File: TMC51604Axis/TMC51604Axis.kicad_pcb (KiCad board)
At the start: 2 copper layers, 63 parts, among them Q1 LTC4359IMS8_PBF, Q2 DMHT6016LFJ, Q3 DMHT6016LFJ, Q4 BSS138, U1 TMC5160-TA

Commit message: sync
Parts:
- removed D1, D11, D12, D2, D5, D6, D7, D8: BAT54, digikey-footprints:SOT-23-3
- C10, C2: footprint Capacitor_SMD:C_0805_2012Metric_Pad1.15x1.40mm_HandSolder -> Capacitor_SMD:C_0603_1608Metric
- C11, C12, C13, C14, C19, C22, C23, C24, C4, C5, C8, C9: footprint Capacitor_SMD:C_0603_1608Metric_Pad1.05x0.95mm_HandSolder -> Capacitor_SMD:C_0603_1608Metric
- C15, C16, C17, C18, C20, C6: footprint Capacitor_SMD:C_1206_3216Metric_Pad1.42x1.75mm_HandSolder -> Capacitor_SMD:C_1206_3216Metric
- D10, D3, D4, D9: footprint Package_TO_SOT_SMD:SOT-23_Handsoldering -> Package_TO_SOT_SMD:SOT-23
- R1: footprint Resistor_SMD:R_1210_3225Metric_Pad1.42x2.65mm_HandSolder -> Resistor_SMD:R_1210_3225Metric
- R10, R19: footprint Resistor_SMD:R_2512_6332Metric_Pad1.52x3.35mm_HandSolder -> Resistor_SMD:R_2512_6332Metric
- R11, R12, R13, R14, R15, R16, R17, R18, R2, R20, R21, R22, R3, R4, R5, R6, R7, R8, R9: footprint Resistor_SMD:R_0805_2012Metric_Pad1.15x1.40mm_HandSolder -> Resistor_SMD:R_0603_1608Metric_Pad1.05x0.95mm_HandSolder
- moved R5 95.4 mm to (182.8, 68.5), turned to 270 degrees
- moved R15 93.5 mm to (179.8, 85.6), turned to 180 degrees
- moved R17 90.7 mm to (176.0, 86.9)
- moved C22 83.9 mm to (179.8, 81.3), turned to 180 degrees
- moved R16 83.6 mm to (179.8, 83.6)
- moved C7 81.0 mm to (55.4, 53.0)
- moved R12 79.6 mm to (176.0, 82.8)
- moved R14 76.5 mm to (176.0, 84.8)
- moved R3 74.8 mm to (176.8, 65.5), turned to 180 degrees
- moved C19 74.5 mm to (162.6, 88.5), turned to 90 degrees
- moved R8 73.5 mm to (180.6, 72.6), turned to 180 degrees
- moved R4 73.0 mm to (180.0, 57.5)
- moved C2 67.9 mm to (158.2, 88.8), turned to 90 degrees
- moved R13 66.8 mm to (164.5, 88.5), turned to 90 degrees
- moved R7 63.5 mm to (171.3, 66.3), turned to 0 degrees
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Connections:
- U1 pad 49: GND -> (no net)
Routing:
- net GND: track 20.2 -> 0.00 mm
- net /MotorDrv1/HB1: track 6.21 -> 0.00 mm
- net Net-(Q2-Pad1): track 7.54 -> 1.98 mm
- net Net-(C3-Pad2): track 0.00 -> 4.90 mm
- net Net-(Q2-Pad4): track 0.00 -> 4.78 mm
- net Net-(C2-Pad1): track 0.00 -> 4.62 mm
- net /MotorDrv1/HA2: track 0.00 -> 4.36 mm
- net +VMotor: track 0.00 -> 4.17 mm
- net Net-(C9-Pad2): track 3.75 -> 0.00 mm
- net Net-(C3-Pad1): track 0.00 -> 3.71 mm
- net Net-(Q3-Pad12): track 0.00 -> 3.50 mm
- net Net-(C2-Pad2): track 0.00 -> 3.05 mm
- net Net-(C19-Pad2): track 0.00 -> 3.04 mm
- net /MotorDrv1/StepperA: track 2.51 -> 0.00 mm
- net Net-(Q2-Pad9): track 0.00 -> 2.33 mm
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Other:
- net class Default: trace_width 0.25 -> 0.28

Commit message: sync
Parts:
- moved R13 22.9 mm to (183.8, 76.1), turned to 180 degrees
- moved Q3 19.1 mm to (184.0, 80.4)
- moved C19 18.7 mm to (151.8, 73.2)
- moved C2 18.7 mm to (147.4, 73.6)
- moved C3 18.7 mm to (149.7, 73.4)
- moved R17 13.0 mm to (186.9, 94.0)
- moved C22 13.0 mm to (190.8, 88.4)
- moved R16 13.0 mm to (190.8, 90.7)
- moved R4 6.65 mm to (183.1, 63.4)
- moved R8 6.52 mm to (175.1, 69.1), turned to 0 degrees
- moved R14 6.04 mm to (178.3, 79.2)
- moved R3 5.01 mm to (179.3, 69.8)
- moved Q2 4.95 mm to (184.1, 67.8)
- moved R2 4.95 mm to (179.2, 65.8)
- moved R5 4.10 mm to (183.3, 72.5), turned to 180 degrees
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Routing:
- net /MotorDrv1/LB1: track 0.00 -> 18.5 mm, vias 0 -> 2
- net /MotorDrv1/LB2: track 0.00 -> 16.9 mm, vias 0 -> 2
- net /MotorDrv1/StepperA: track 0.00 -> 11.3 mm
- net /MotorDrv1/HB2: track 0.00 -> 10.9 mm, vias 0 -> 2
- net /MotorDrv1/StepperB: track 0.00 -> 10.9 mm
- net /MotorDrv1/HB1: track 0.00 -> 10.7 mm, vias 0 -> 2
- net Net-(C9-Pad2): track 0.00 -> 8.27 mm
- net Net-(R8-Pad1): track 0.00 -> 6.60 mm
- net Net-(R7-Pad1): track 0.00 -> 6.23 mm
- net Net-(C5-Pad2): track 0.00 -> 4.94 mm
- net Net-(Q2-Pad4): track 4.78 -> 2.57 mm

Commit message: Layout done! Still untested
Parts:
- removed C8: 10uF, Capacitor_SMD:C_0603_1608Metric
- added C25: 2.2u, Capacitor_SMD:C_0603_1608Metric, F.Cu at (104.4, 92.5)
- added C26: 470n, Capacitor_SMD:C_0603_1608Metric, F.Cu at (102.5, 109.0)
- added C27: 100n, Capacitor_SMD:C_0603_1608Metric, F.Cu at (96.5, 101.5)
- added C28: 1n/100V, Capacitor_SMD:C_0603_1608Metric, B.Cu at (136.4, 94.9)
- added C29: 1n/100V, Capacitor_SMD:C_0603_1608Metric, B.Cu at (136.7, 98.9)
- added C30: 1n/100V, Capacitor_SMD:C_0603_1608Metric, B.Cu at (136.7, 103.3)
- added C31: 1n/100V, Capacitor_SMD:C_0603_1608Metric, B.Cu at (136.3, 107.4)
- added C32: 2n2, Capacitor_SMD:C_0603_1608Metric, F.Cu at (116.5, 88.5)
- added C33: 100n, Capacitor_SMD:C_0603_1608Metric, F.Cu at (129.4, 89.2)
- added C34: 100n, Capacitor_SMD:C_0603_1608Metric, F.Cu at (94.4, 92.6)
- added C35: 470n, Capacitor_SMD:C_0603_1608Metric, F.Cu at (113.5, 109.6)
- added C36: 470n, Capacitor_SMD:C_0603_1608Metric, F.Cu at (113.5, 102.9)
- added C37: 15pF, peters:D_0805_peter, F.Cu at (98.2, 90.9)
- added C38: 470n/100V, Capacitor_SMD:C_1206_3216Metric, F.Cu at (118.5, 106.2)
- added C39: 220uF/100V, Capacitor_SMD:CP_Elec_10x14.3, F.Cu at (122.4, 121.7)
- added C40: 2n2, Capacitor_SMD:C_0603_1608Metric, F.Cu at (116.3, 113.5)
- added C41: 100n, Capacitor_SMD:C_0603_1608Metric, F.Cu at (130.0, 112.6)
- added C42: 10u, peters:C_0805_peter, B.Cu at (85.6, 125.7)
- added C43: 100n, peters:C_0805_peter, B.Cu at (109.1, 114.4)
- added C44: 100n, peters:C_0805_peter, B.Cu at (91.8, 103.6)
- added C45: 100n, peters:C_0805_peter, B.Cu at (95.2, 114.6)
- added D1: 1N4148W, Diode_SMD:D_SOD-123, B.Cu at (101.1, 76.2)
- added D11: LED, peters:D_0805__HandSolder_peter, F.Cu at (80.8, 97.9)
- added D12: LED, peters:D_0805__HandSolder_peter, F.Cu at (85.7, 97.9)
- added D13: LED, peters:D_0805__HandSolder_peter, F.Cu at (88.1, 97.9)
- added D14: LED, peters:D_0805__HandSolder_peter, F.Cu at (83.2, 97.9)
- added D15: LED, peters:D_0805__HandSolder_peter, F.Cu at (90.0, 118.5)
- added D16: LED, peters:D_0805__HandSolder_peter, F.Cu at (82.8, 118.5)
- added D17: LED, peters:D_0805__HandSolder_peter, F.Cu at (80.4, 118.5)
- added D18: LED, peters:D_0805__HandSolder_peter, F.Cu at (85.2, 118.5)
- added D19: LED, peters:D_0805__HandSolder_peter, F.Cu at (87.6, 118.5)
- added D2: 7V, Diode_SMD:D_1206_3216Metric, B.Cu at (106.6, 76.2)
- added D20: BAT54S, Package_TO_SOT_SMD:SOT-23, B.Cu at (78.0, 110.4)
- added D21: BAT54S, Package_TO_SOT_SMD:SOT-23, B.Cu at (81.4, 101.7)
- added D22: BAT54S, Package_TO_SOT_SMD:SOT-23, B.Cu at (77.6, 90.0)
- added D23: BAT54S, Package_TO_SOT_SMD:SOT-23, B.Cu at (81.4, 90.0)
- added D24: BAT54S, Package_TO_SOT_SMD:SOT-23, B.Cu at (77.3, 101.7)
- added D25: BAT54S, Package_TO_SOT_SMD:SOT-23, B.Cu at (86.5, 121.8)
- added D26: BAT54S, Package_TO_SOT_SMD:SOT-23, B.Cu at (77.5, 122.4)
- added D27: BAT54S, Package_TO_SOT_SMD:SOT-23, B.Cu at (91.1, 121.8)
- added D28: BAT54S, Package_TO_SOT_SMD:SOT-23, B.Cu at (95.6, 121.8)
- added D29: BAT54S, Package_TO_SOT_SMD:SOT-23, B.Cu at (81.5, 122.4)
- added D5: LT1766, Package_SO:TSSOP-16-1EP_4.4x5mm_P0.65mm, B.Cu at (92.5, 71.5)
- added D6: D_Schottky, Diode_SMD:D_SOD-123F, B.Cu at (92.6, 66.5)
- added D7: ZHCS1006TA, Package_TO_SOT_SMD:SOT-23, F.Cu at (107.7, 88.3)
- added D8: ZHCS1006TA, Package_TO_SOT_SMD:SOT-23, F.Cu at (111.5, 88.3)
- added F1: Fuse, Fuse:Fuse_2512_6332Metric, F.Cu at (80.6, 76.2)
- added FB2: MPZ2012S601A, Resistor_SMD:R_0805_2012Metric_Pad1.15x1.40mm_HandSolder, B.Cu at (91.7, 76.8)
- added H1: MountingHole, MountingHole:MountingHole_3.2mm_M3, F.Cu at (81.7, 66.9)
- added H2: MountingHole, MountingHole:MountingHole_3.2mm_M3, F.Cu at (134.4, 130.6)
- added H3: MountingHole, MountingHole:MountingHole_3.2mm_M3, F.Cu at (134.4, 66.9)
- added H4: MountingHole, MountingHole:MountingHole_3.2mm_M3, F.Cu at (64.4, 130.6)
- added J1: +48Vin, Connector_Phoenix_MSTB:PhoenixContact_MSTB_2,5_2-GF_1x02_P5.00mm_Horizontal_ThreadedFlange_MountHole, F.Cu at (71.1, 70.9)
- added J2: Stepper_conn, TerminalBlock_Phoenix:TerminalBlock_Phoenix_PT-1,5-4-3.5-H_1x04_P3.50mm_Horizontal, F.Cu at (133.9, 95.9)
- added J3: RJ45_Shielded, peters:360s-1812-11001(RJ45), F.Cu at (69.3, 115.6)
- added J4: EncCon1, TerminalBlock_Phoenix:TerminalBlock_Phoenix_PT-1,5-3-3.5-H_1x03_P3.50mm_Horizontal, F.Cu at (92.2, 130.2)
- added J5: RJ45_Shielded, peters:360s-1812-11001(RJ45), F.Cu at (69.3, 95.4)
- added J6: EncCon2, TerminalBlock_Phoenix:TerminalBlock_Phoenix_PT-1,5-3-3.5-H_1x03_P3.50mm_Horizontal, F.Cu at (103.9, 130.2)
- added JP1: SPI_MODE, Jumper:SolderJumper-3_P2.0mm_Open_TrianglePad1.0x1.5mm, F.Cu at (123.1, 129.9)
- added JP2: SD_MODE, Jumper:SolderJumper-3_P2.0mm_Open_TrianglePad1.0x1.5mm, F.Cu at (111.4, 129.8)
- added JP3: Encoder_Voltage_Sel, Jumper:SolderJumper-3_P2.0mm_Open_TrianglePad1.0x1.5mm, F.Cu at (75.8, 129.9)
- added L1: 33uH, Inductor_SMD:L_7.3x7.3_H3.5, B.Cu at (105.0, 70.1)
- added R23: 12R, Resistor_SMD:R_0603_1608Metric, F.Cu at (119.5, 108.3)
- added R24: 12R, Resistor_SMD:R_0603_1608Metric, F.Cu at (119.5, 101.9)
- added R25: 12R, Resistor_SMD:R_0603_1608Metric, F.Cu at (119.5, 110.6)
- added R26: 47R, Resistor_SMD:R_0603_1608Metric, F.Cu at (119.5, 112.5)
- added R27: 0R1, Resistor_SMD:R_1206_3216Metric, F.Cu at (126.9, 112.8)
- added R28: 47R, Resistor_SMD:R_0603_1608Metric, F.Cu at (119.5, 114.6)
- added R29: 100K, Resistor_SMD:R_0603_1608Metric, F.Cu at (99.2, 110.6)
- added R30: 100K, Resistor_SMD:R_0603_1608Metric, F.Cu at (96.0, 113.2)
- added R31: 2k2, peters:R_0805_peter, F.Cu at (80.8, 102.9)
- added R32: 2k2, peters:R_0805_peter, F.Cu at (85.7, 102.9)
- added R33: 100R, peters:R_0805_peter, B.Cu at (73.2, 113.3)
- added R34: 100R, peters:R_0805_peter, B.Cu at (73.4, 97.3)
- added R35: 100R, peters:R_0805_peter, B.Cu at (73.4, 92.8)
- added R36: 100R, peters:R_0805_peter, B.Cu at (73.4, 95.1)
- added R37: 100R, peters:R_0805_peter, B.Cu at (73.4, 99.6)
- added R38: 100R, peters:R_0805_peter, B.Cu at (88.8, 125.7)
- added R39: 100R, peters:R_0805_peter, B.Cu at (72.9, 119.9)
- added R40: 100R, peters:R_0805_peter, B.Cu at (92.3, 125.7)
- added R41: 2k2, peters:R_0805_peter, F.Cu at (88.1, 102.9)
- added R42: 2k2, peters:R_0805_peter, F.Cu at (83.3, 102.9)
- added R43: 2k2, peters:R_0805_peter, F.Cu at (90.0, 122.7)
- added R44: 2k2, peters:R_0805_peter, F.Cu at (82.7, 122.7)
- added R45: 2k2, peters:R_0805_peter, F.Cu at (80.4, 122.7)
- added R46: 2k2, peters:R_0805_peter, F.Cu at (85.2, 122.7)
- added R47: 2k2, peters:R_0805_peter, F.Cu at (87.6, 122.7)
- added R48: 100R, peters:R_0805_peter, B.Cu at (97.2, 125.6)
- added R49: 100R, peters:R_0805_peter, B.Cu at (72.9, 117.6)
- added TP1: TestPoint, TestPoint:TestPoint_Pad_1.5x1.5mm, F.Cu at (86.7, 70.9)
- added TP2: TestPoint, TestPoint:TestPoint_Pad_1.5x1.5mm, F.Cu at (92.8, 70.9)
- added TP3: spare, TestPoint:TestPoint_THTPad_1.0x1.0mm_Drill0.5mm, F.Cu at (100.5, 123.2)
- added TP4: TestPoint, TestPoint:TestPoint_Pad_1.5x1.5mm, F.Cu at (108.3, 82.8)
- added TP5: TestPoint, TestPoint:TestPoint_Pad_1.5x1.5mm, F.Cu at (101.2, 82.8)
- added TP6: TestPoint, TestPoint:TestPoint_Pad_1.5x1.5mm, F.Cu at (104.5, 82.8)
- added TP7: TestPoint, TestPoint:TestPoint_Pad_1.5x1.5mm, F.Cu at (112.3, 82.7)
- added U2: LM2937, Package_TO_SOT_SMD:SOT-223-3_TabPin2, B.Cu at (82.8, 81.8)
- added U3: TMC5160A-TA, peters:LQFP-48-1EP_7x7mm_P0.5mm_EP3.6x3.6mm_peter, F.Cu at (104.3, 100.7)
- added U4: ASDMB-12.0MHz, Oscillator:Oscillator_SMD_Abracon_ASDMB-4Pin_2.5x2.0mm, F.Cu at (98.3, 93.9)
- added U5: 74LVC125, Package_SO:SO-14_5.3x10.2mm_P1.27mm, B.Cu at (102.6, 111.8)
- added U6: 74LVC125, Package_SO:SO-14_5.3x10.2mm_P1.27mm, B.Cu at (88.9, 96.8)
- added U7: 74LVC125, Package_SO:SO-14_5.3x10.2mm_P1.27mm, B.Cu at (88.9, 111.6)
- C1: value 4,7uF -> 330n; footprint Capacitor_SMD:C_1210_3225Metric_Pad1.42x2.65mm_HandSolder -> peters:C_0805_peter; moved to B.Cu
- C10: value 2.2u -> 10u; moved to B.Cu
- C11: value 470n -> 1uF; footprint Capacitor_SMD:C_0603_1608Metric -> peters:C_0805_peter; moved to B.Cu
- C12: value 100n -> 100p; footprint Capacitor_SMD:C_0603_1608Metric -> peters:C_0805_peter; moved to B.Cu
- C13: value 2n2 -> 220p; footprint Capacitor_SMD:C_0603_1608Metric -> peters:C_0805_peter; moved to B.Cu
- C14: value 100n -> 22nF; footprint Capacitor_SMD:C_0603_1608Metric -> peters:C_0805_peter; moved to B.Cu
- C15: value 1n/100V -> 100n/100v; footprint Capacitor_SMD:C_1206_3216Metric -> Capacitor_SMD:C_1210_3225Metric_Pad1.42x2.65mm_HandSolder
- C16: value 1n/100V -> 4,7uF/100v; footprint Capacitor_SMD:C_1206_3216Metric -> Capacitor_SMD:C_1210_3225Metric_Pad1.42x2.65mm_HandSolder
- C17: value 1n/100V -> 22n/100v; footprint Capacitor_SMD:C_1206_3216Metric -> Capacitor_SMD:C_0603_1608Metric
- C18: value 1n/100V -> 100n/100V; footprint Capacitor_SMD:C_1206_3216Metric -> peters:C_0805_peter
- C19: value 470n -> 220n/100v
- C2: value 22n/100v -> 10p; footprint Capacitor_SMD:C_0603_1608Metric -> peters:C_0805_peter
- C21: footprint Capacitor_THT:C_Radial_D16.0mm_H25.0mm_P7.50mm -> Capacitor_SMD:CP_Elec_10x14.3
- C23: value 2n2 -> 2.2uF
- C24: value 100n -> 470n
- C3: value 100n/100V -> 10uF/100v; footprint Capacitor_SMD:C_0805_2012Metric_Pad1.15x1.40mm_HandSolder -> Capacitor_SMD:CP_Elec_8x6.2
- C4: value 220n -> 22uF/100v; footprint Capacitor_SMD:C_0603_1608Metric -> Capacitor_SMD:CP_Elec_8x6.2
- C5: value 470n -> 47nF; footprint Capacitor_SMD:C_0603_1608Metric -> peters:C_0805_peter
- C6: value 470n/100V -> 2.2uF; footprint Capacitor_SMD:C_1206_3216Metric -> peters:C_0805_peter; moved to B.Cu
- C7: value 220uF/100V -> 47u/25V; footprint Capacitor_THT:C_Radial_D16.0mm_H25.0mm_P7.50mm -> Capacitor_THT:CP_Radial_D10.0mm_P5.00mm
- C9: value 470n -> 100n; moved to B.Cu
- D3: value ZHCS1006TA -> 10V; footprint Package_TO_SOT_SMD:SOT-23 -> Diode_SMD:D_1206_3216Metric
- D4: value ZHCS1006TA -> LED; footprint Package_TO_SOT_SMD:SOT-23 -> Diode_SMD:D_0805_2012Metric
- Q1: value LTC4359IMS8_PBF -> SUD08P06-155L; footprint digikey-footprints:TSSOP-8_W3mm -> Package_TO_SOT_SMD:TO-252-2
- R1: value 1R -> 0R01; footprint Resistor_SMD:R_1210_3225Metric -> Resistor_SMD:R_2512_6332Metric
- R10: value 0R1 -> 12R; footprint Resistor_SMD:R_2512_6332Metric -> Resistor_SMD:R_0603_1608Metric
- R11: value 47R -> 12R; footprint Resistor_SMD:R_0603_1608Metric_Pad1.05x0.95mm_HandSolder -> Resistor_SMD:R_0603_1608Metric
- R12: value 12R -> 0R; footprint Resistor_SMD:R_0603_1608Metric_Pad1.05x0.95mm_HandSolder -> Resistor_SMD:R_0603_1608Metric
- R13, R14: footprint Resistor_SMD:R_0603_1608Metric_Pad1.05x0.95mm_HandSolder -> Resistor_SMD:R_0603_1608Metric
- R15: value 12R -> 47R; footprint Resistor_SMD:R_0603_1608Metric_Pad1.05x0.95mm_HandSolder -> Resistor_SMD:R_0603_1608Metric
- R16: value 0R -> 0R1; footprint Resistor_SMD:R_0603_1608Metric_Pad1.05x0.95mm_HandSolder -> Resistor_SMD:R_1206_3216Metric
- R17: value 0R -> 47R; footprint Resistor_SMD:R_0603_1608Metric_Pad1.05x0.95mm_HandSolder -> Resistor_SMD:R_0603_1608Metric
- R18: value 47R -> 100k; footprint Resistor_SMD:R_0603_1608Metric_Pad1.05x0.95mm_HandSolder -> peters:R_0805_peter
- R19: value 0R1 -> NC; footprint Resistor_SMD:R_2512_6332Metric -> peters:R_0805_peter
- R2: value 12R -> 36K5; footprint Resistor_SMD:R_0603_1608Metric_Pad1.05x0.95mm_HandSolder -> peters:R_0805_peter; moved to B.Cu
- R20, R9: value 47R -> 0R; footprint Resistor_SMD:R_0603_1608Metric_Pad1.05x0.95mm_HandSolder -> Resistor_SMD:R_0603_1608Metric
- R21: value 100K -> 0R; footprint Resistor_SMD:R_0603_1608Metric_Pad1.05x0.95mm_HandSolder -> Resistor_SMD:R_0603_1608Metric
- R22: value 100K -> 12R; footprint Resistor_SMD:R_0603_1608Metric_Pad1.05x0.95mm_HandSolder -> Resistor_SMD:R_0603_1608Metric
- R3: value 12R -> 100k; footprint Resistor_SMD:R_0603_1608Metric_Pad1.05x0.95mm_HandSolder -> peters:R_0805_peter
- R4: value 12R -> 10K; footprint Resistor_SMD:R_0603_1608Metric_Pad1.05x0.95mm_HandSolder -> peters:R_0805_peter
- R5: value 12R -> 4K12; footprint Resistor_SMD:R_0603_1608Metric_Pad1.05x0.95mm_HandSolder -> peters:R_0805_peter; moved to B.Cu
- R6: value 2R2 -> 2k2; footprint Resistor_SMD:R_0603_1608Metric_Pad1.05x0.95mm_HandSolder -> peters:R_0805_peter; moved to B.Cu
- R7: value 0R -> 1R; footprint Resistor_SMD:R_0603_1608Metric_Pad1.05x0.95mm_HandSolder -> peters:R_0805_peter
- R8: value 0R -> 2R2; footprint Resistor_SMD:R_0603_1608Metric_Pad1.05x0.95mm_HandSolder -> Resistor_SMD:R_0603_1608Metric
- U1: value TMC5160-TA -> AP2210-3.3V; footprint Package_QFP:TQFP-48-1EP_7x7mm_P0.5mm_EP5x5mm_ThermalVias -> Package_TO_SOT_SMD:SOT-23-5_HandSoldering; moved to B.Cu
- moved R5 98.9 mm to (84.3, 72.5), turned to 270 degrees
- moved R4 93.0 mm to (90.2, 65.4)
- moved R2 92.8 mm to (86.6, 72.5), turned to 90 degrees
- moved C9 90.0 mm to (85.6, 76.5)
- moved R3 89.7 mm to (91.7, 89.0), turned to 0 degrees
- moved R7 85.9 mm to (102.6, 113.3), turned to 270 degrees
- moved C5 84.2 mm to (92.1, 83.4)
- moved C22 77.9 mm to (113.7, 99.3)
- moved R8 76.1 mm to (102.7, 92.6), turned to 90 degrees
- moved Q4 75.4 mm to (98.9, 113.3)
- moved C15 75.4 mm to (105.2, 118.4), turned to 270 degrees
- moved U1 74.5 mm to (91.6, 81.2), turned to 0 degrees
- moved R17 67.7 mm to (119.5, 87.6), turned to 180 degrees
- moved C21 67.7 mm to (122.4, 80.6)
- moved R13 66.0 mm to (119.5, 91.3), turned to 0 degrees
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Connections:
- C1 pad 1: +VMotor -> Net-(C1-Pad1)
- C1 pad 2: GND -> Net-(C1-Pad2)
- C10 pad 1: Net-(C10-Pad1) -> +5V
- C11 pad 1: Net-(C11-Pad1) -> +5V
- C12 pad 1: GND -> Net-(C12-Pad1)
- C12 pad 2: +3V3 -> GND
- C13 pad 2: Net-(C13-Pad2) -> GND
- C14 pad 1: GND -> Net-(C14-Pad1)
- C14 pad 2: Net-(C14-Pad2) -> GND
- C15 pad 1: /MotorDrv1/StepperA -> +48V
- C16 pad 1: /MotorDrv1/StepperB -> +48V
- C17 pad 1: /MotorDrv1/StepperC -> Net-(C17-Pad1)
- C17 pad 2: GND -> Net-(C17-Pad2)
- C18 pad 1: /MotorDrv1/StepperD -> Net-(C18-Pad1)
- C18 pad 2: GND -> Net-(C18-Pad2)
- C19 pad 1: /MotorDrv1/StepperD -> Net-(C18-Pad1)
- C19 pad 2: Net-(C19-Pad2) -> GND
- C2 pad 1: Net-(C2-Pad1) -> +48V
- C20 pad 1: +VMotor -> +48V
- C21 pad 1: +VMotor -> +48V
- C22 pad 1: /MotorDrv1/StepperC -> /MotorDrv1/StepperB
- C23 pad 1: Net-(C23-Pad1) -> +12V
- C23 pad 2: Net-(C23-Pad2) -> GND
- C24 pad 1: GND -> /MotorDrv1/StepperA
- C3 pad 1: Net-(C3-Pad1) -> +48V
- C3 pad 2: Net-(C3-Pad2) -> GND
- C4 pad 1: Net-(C3-Pad1) -> +48V
- C5 pad 1: /MotorDrv1/StepperB -> Net-(C2-Pad2)
- C5 pad 2: Net-(C5-Pad2) -> GND
- C6 pad 1: +VMotor -> +3V3
- C7 pad 1: +VMotor -> +12V
- C9 pad 1: /MotorDrv1/StepperA -> Net-(C9-Pad1)
- C9 pad 2: Net-(C9-Pad2) -> GND
- D3 pad 1: /MotorDrv1/StepperB -> Net-(C2-Pad2)
- D3 pad 2: (no net) -> Net-(D3-Pad2)
- D4 pad 1: /MotorDrv1/StepperA -> Net-(D4-Pad1)
- D4 pad 2: (no net) -> +48V
- Q1 pad 1: (no net) -> Net-(D3-Pad2)
- Q1 pad 2: (no net) -> Net-(F1-Pad1)
- Q1 pad 3: (no net) -> Net-(C2-Pad2)
- Q2 pad 11: +VMotor -> +48V
- Q2 pad 13: +VMotor -> +48V
- Q2 pad 2: +VMotor -> +48V
- Q2 pad 5: Net-(C14-Pad2) -> Net-(C33-Pad2)
- Q2 pad 6: Net-(C14-Pad2) -> Net-(C33-Pad2)
- Q2 pad 7: Net-(C14-Pad2) -> Net-(C33-Pad2)
- Q2 pad 8: Net-(C14-Pad2) -> Net-(C33-Pad2)
- Q3 pad 11: +VMotor -> +48V
- Q3 pad 13: +VMotor -> +48V
- Q3 pad 2: +VMotor -> +48V
- Q3 pad 5: Net-(C24-Pad2) -> Net-(C41-Pad2)
- Q3 pad 6: Net-(C24-Pad2) -> Net-(C41-Pad2)
- Q3 pad 7: Net-(C24-Pad2) -> Net-(C41-Pad2)
- Q3 pad 8: Net-(C24-Pad2) -> Net-(C41-Pad2)
- R1 pad 1: +VMotor -> Net-(C2-Pad2)
- R1 pad 2: Net-(C3-Pad1) -> +48V
- R10 pad 1: Net-(C14-Pad2) -> /MotorDrv1/HB1
- R10 pad 2: GND -> Net-(Q2-Pad1)
- R11 pad 1: GND -> Net-(Q2-Pad12)
- R11 pad 2: Net-(C13-Pad1) -> /MotorDrv1/HB2
- R12 pad 1: /MotorDrv1/HA1 -> Net-(R12-Pad1)
- R12 pad 2: Net-(Q3-Pad1) -> /MotorDrv1/StepperB
- R13 pad 1: Net-(Q3-Pad12) -> /MotorDrv1/LB1
- R13 pad 2: /MotorDrv1/HA2 -> Net-(Q2-Pad4)
- R14 pad 1: /MotorDrv1/LA1 -> Net-(Q2-Pad9)
- R14 pad 2: Net-(Q3-Pad4) -> /MotorDrv1/LB2
- R15 pad 1: Net-(Q3-Pad9) -> Net-(C33-Pad2)
- R15 pad 2: /MotorDrv1/LA2 -> Net-(C32-Pad2)
- R16 pad 1: Net-(R16-Pad1) -> Net-(C33-Pad2)
- R16 pad 2: /MotorDrv1/StepperC -> GND
- R17 pad 1: Net-(R17-Pad1) -> GND
- R17 pad 2: /MotorDrv1/StepperD -> Net-(C32-Pad1)
- R18 pad 1: Net-(C24-Pad2) -> +3V3
- R18 pad 2: Net-(C23-Pad2) -> Net-(R18-Pad2)
- R19 pad 1: Net-(C24-Pad2) -> GND
- R19 pad 2: GND -> Net-(C37-Pad1)
- R2 pad 1: /MotorDrv1/HB1 -> +12V
- R2 pad 2: Net-(Q2-Pad1) -> Net-(D5-Pad12)
- R20 pad 1: GND -> Net-(R20-Pad1)
- R20 pad 2: Net-(C23-Pad1) -> /MotorDrv1/StepperC
- R21 pad 1: Net-(Q4-Pad3) -> Net-(R21-Pad1)
- R21 pad 2: +3V3 -> /MotorDrv1/StepperD
- R22 pad 1: GND -> /MotorDrv1/HA1
- R22 pad 2: /MotorDrv1/DRV_ENA -> Net-(Q3-Pad1)
- R3 pad 1: Net-(Q2-Pad12) -> Net-(D3-Pad2)
- R3 pad 2: /MotorDrv1/HB2 -> GND
- R4 pad 1: /MotorDrv1/LB1 -> Net-(D4-Pad1)
- R4 pad 2: Net-(Q2-Pad4) -> GND
- R5 pad 1: Net-(Q2-Pad9) -> Net-(D5-Pad12)
- R5 pad 2: /MotorDrv1/LB2 -> GND
- R6 pad 1: Net-(C10-Pad1) -> Net-(C13-Pad1)
- R6 pad 2: Net-(C11-Pad1) -> Net-(C14-Pad1)
- R7 pad 1: Net-(R7-Pad1) -> Net-(C18-Pad1)
- R7 pad 2: /MotorDrv1/StepperA -> +48V
- R8 pad 1: Net-(R8-Pad1) -> Net-(C25-Pad1)
- R8 pad 2: /MotorDrv1/StepperB -> Net-(C26-Pad1)
- R9 pad 1: Net-(C14-Pad2) -> Net-(R9-Pad1)
- R9 pad 2: Net-(C13-Pad2) -> /MotorDrv1/StepperA
- U1 pad 1: /MotorDrv1/HB1 -> +5V
- U1 pad 2: Net-(C9-Pad2) -> GND
- U1 pad 3: +12V -> +5V
- U1 pad 4: +12V -> Net-(C12-Pad1)
- U1 pad 5: Net-(C10-Pad1) -> +3V3
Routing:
- net GND: track 0.00 -> 292.5 mm, vias 0 -> 125
- net +5V: track 0.00 -> 116.4 mm, vias 0 -> 3
- net +12V: track 0.00 -> 71.1 mm, vias 0 -> 2
- net +48V: track 0.00 -> 62.0 mm, vias 0 -> 58
- net +3V3: track 0.00 -> 56.0 mm, vias 0 -> 21
- net /MotorDrv1/CLK: track 0.00 -> 53.1 mm, vias 0 -> 4
- net /MotorDrv1/StepperC: track 0.00 -> 49.1 mm, vias 0 -> 7
- net Net-(JP1-Pad2): track 0.00 -> 45.9 mm, vias 0 -> 2
- net Net-(C40-Pad1): track 0.00 -> 45.6 mm, vias 0 -> 2
- net /MotorDrv1/REFL_STEP: track 0.00 -> 45.1 mm, vias 0 -> 1
- net /Inputs/DIR_REFR: track 0.00 -> 44.2 mm, vias 0 -> 5
- net Net-(C40-Pad2): track 0.00 -> 42.9 mm, vias 0 -> 2
- net /MotorDrv1/MOSI: track 0.00 -> 42.0 mm, vias 0 -> 1
- net /Inputs/enc_volt: track 0.00 -> 39.3 mm, vias 0 -> 1
- net /MotorDrv1/StepperD: track 0.00 -> 38.0 mm, vias 0 -> 5
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- added copper zone on B.Cu, net +3V3
- added copper zone on In2.Cu, net +3V3
- added copper zone on B.Cu, net +48V
- added copper zone on F.Cu, net +48V
- added copper zone on B.Cu, net /MotorDrv1/StepperA
- added copper zone on B.Cu, net /MotorDrv1/StepperB
- added copper zone on B.Cu, net /MotorDrv1/StepperC
- added copper zone on B.Cu, net /MotorDrv1/StepperD
- added copper zone on B.Cu, net GND
- added copper zone on F.Cu, net GND
- added copper zone on In1.Cu, net GND
- added copper zone on F.Cu, net Net-(C2-Pad2)
- added copper zone on B.Cu, net Net-(C33-Pad2)
- added copper zone on F.Cu, net Net-(C33-Pad2)
- added copper zone on B.Cu, net Net-(C41-Pad2)
- added copper zone on F.Cu, net Net-(C41-Pad2)
- added copper zone on F.Cu, net Net-(F1-Pad1)
- added copper zone on F.Cu, net Net-(F1-Pad2)
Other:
- board outline added: 77.7 x 72.8 mm
- copper layers 2 -> 4
- net class Default: trace_width 0.28 -> 0.25; via_dia 0.8 -> 0.6; via_drill 0.4 -> 0.3
- rule via_min_size: 0.4 -> 0.45
- board text added: "+48VDC IN"
- board text added: "12"
- board text added: "3,3"
- board text added: "3.3"
- board text added: "5"
- board text added: "5.0"
- board text added: "A"
- board text added: "B"
- board text added: "C"
- board text added: "CSN"
- board text added: "D"
- board text added: "DIAG_SWn"
- board text added: "DIAG_SWp"
- board text added: "DIR_REF_R"
- board text added: "ENA"
- board text added: "ENCODER"
- board text added: "ENC_VOLT"
- board text added: "GND"
- board text added: "JLCJLCJLCJLC"
- board text added: "N"
- board text added: "SCK"
- board text added: "SDI"
- board text added: "SDO"
- board text added: "SD_MODE"
- board text added: "SPI"
- board text added: "SPI IN"
- board text added: "SPI_MODE"
- board text added: "STEP/DIR IN"
- board text added: "STEPPER OUT"
- board text added: "STEP_REF_L"
- board text added: "Spare"
- board text added: "VCC"

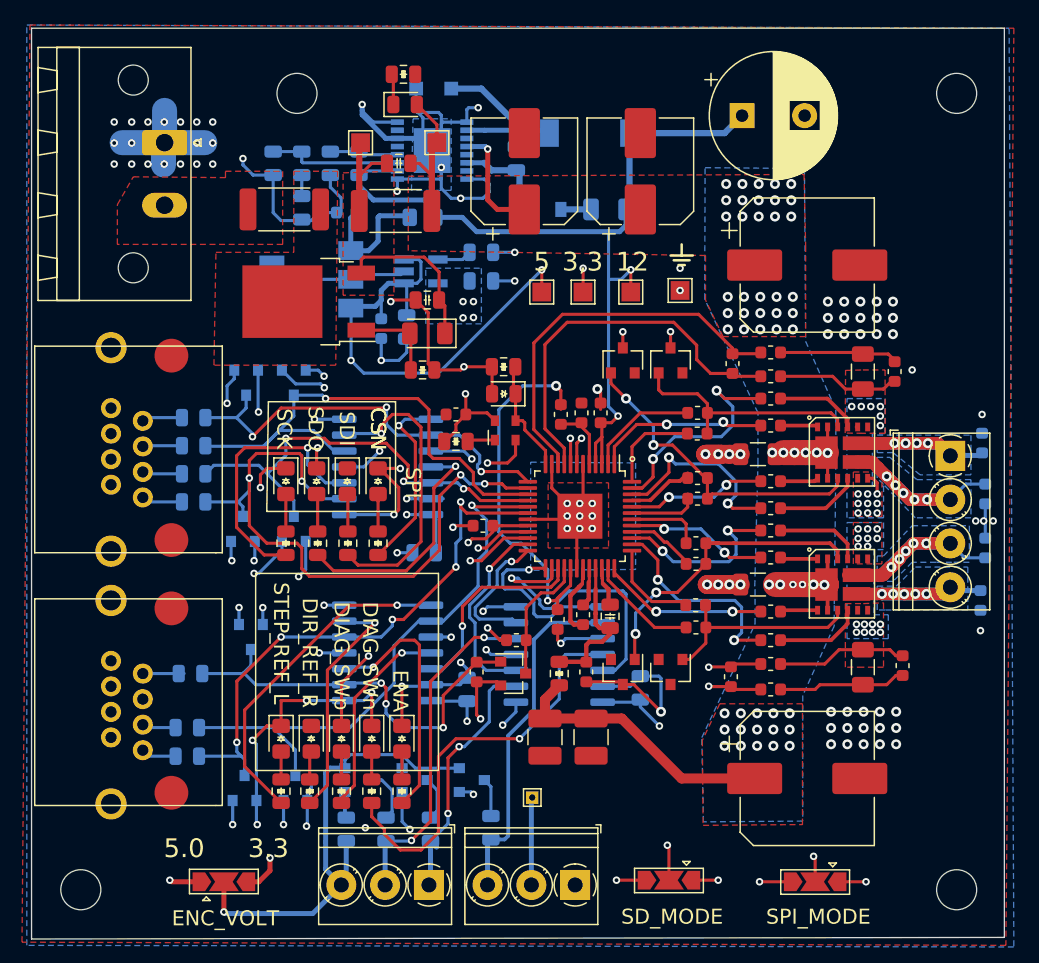
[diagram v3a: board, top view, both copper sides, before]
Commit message: Redone input section
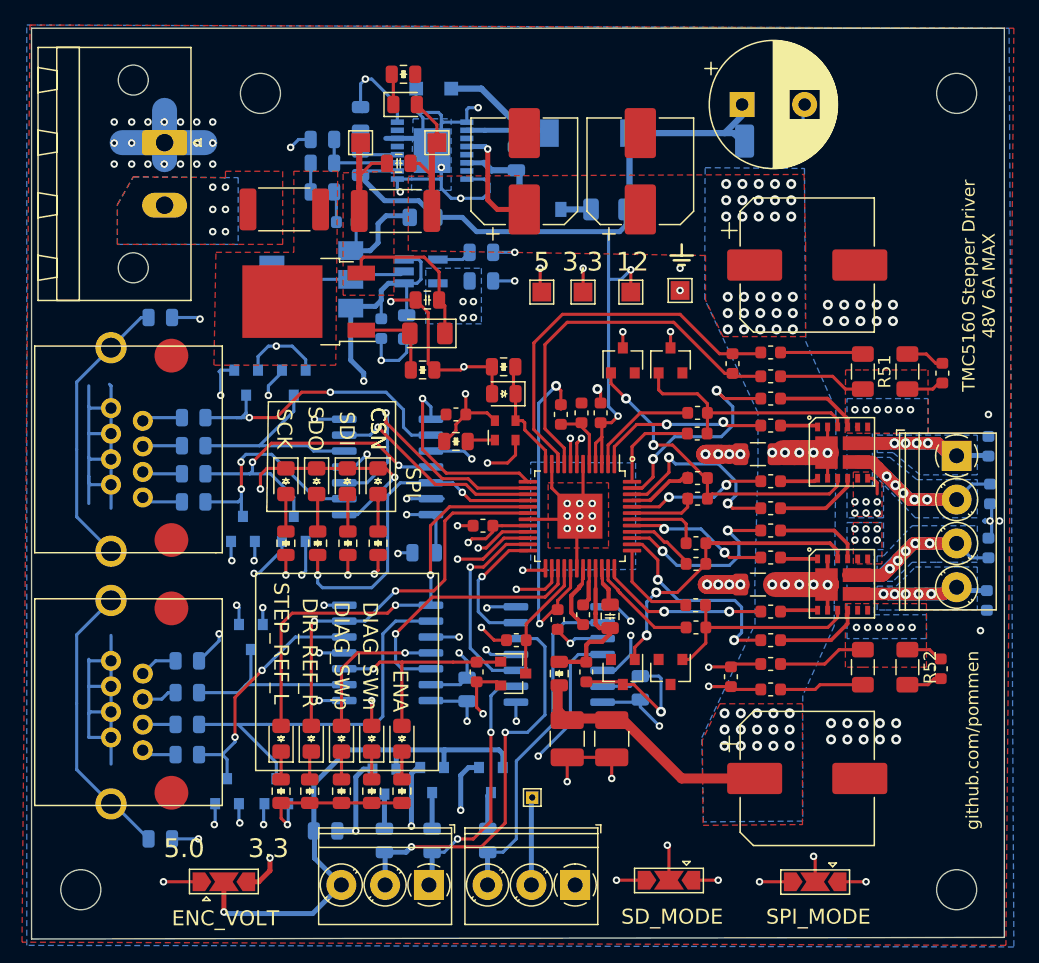
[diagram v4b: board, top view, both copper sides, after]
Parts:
- added C46: 100n, peters:C_0805_peter, B.Cu at (70.7, 126.5)
- added C47: 100n, peters:C_0805_peter, B.Cu at (70.7, 84.8)
- added C8: 47u/25, Capacitor_SMD:C_2010_5025Metric_Pad1.52x2.65mm_HandSolder, B.Cu at (119.8, 70.7)
- added R50: 20R, peters:R_0805_peter, B.Cu at (72.9, 112.3)
- added R51: 0R1, Resistor_SMD:R_1206_3216Metric, F.Cu at (130.4, 89.2)
- added R52: 0R1, Resistor_SMD:R_1206_3216Metric, F.Cu at (130.4, 112.8)
- moved C13 4.37 mm to (83.7, 70.6), turned to 180 degrees
- moved R5 4.30 mm to (86.7, 69.0), turned to 90 degrees
- moved C33 3.81 mm to (133.2, 89.3)
- moved C41 3.06 mm to (133.1, 112.9)
- moved H1 2.92 mm to (78.7, 66.9)
- moved D25 2.16 mm to (88.6, 121.9), turned to 270 degrees
- moved C14 2.08 mm to (83.7, 74.8), turned to 0 degrees
- moved C16 1.78 mm to (103.3, 118.5)
- moved C15 1.66 mm to (106.8, 118.5)
- moved C42 1.66 mm to (83.9, 125.9), turned to 0 degrees
- moved R6 1.65 mm to (83.7, 72.5), turned to 180 degrees
- moved D29 1.55 mm to (80.0, 122.7)
- moved R33 1.55 mm to (72.9, 114.8)
- moved D28 1.52 mm to (97.2, 121.8), turned to 270 degrees
- moved D26 1.42 mm to (76.1, 122.7)
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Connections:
- net /Inputs/DIR_REFR_raw renamed Net-(J3-Pad8)
- net /Inputs/STEP_REFL_raw renamed Net-(J3-Pad6)
- D15 pad 1: GND -> Net-(D15-Pad1)
- D15 pad 2: Net-(D15-Pad2) -> /MotorDrv1/DRV_ENA
- D16 pad 1: GND -> Net-(D16-Pad1)
- D16 pad 2: Net-(D16-Pad2) -> /Inputs/DIR_REFR
- D17 pad 1: GND -> Net-(D17-Pad1)
- D17 pad 2: Net-(D17-Pad2) -> /MotorDrv1/REFL_STEP
- D18 pad 1: GND -> Net-(D18-Pad1)
- D19 pad 1: GND -> Net-(D19-Pad1)
- D20 pad 2: +3V3 -> /Inputs/Signal_VCC
- D20 pad 3: /MotorDrv1/DRV_ENA -> Net-(D20-Pad3)
- D21 pad 2: +3V3 -> /Inputs/Signal_VCC
- D21 pad 3: /MotorDrv1/MISO -> Net-(D21-Pad3)
- D22 pad 2: +3V3 -> /Inputs/Signal_VCC
- D22 pad 3: /Inputs/CSN -> Net-(D22-Pad3)
- D23 pad 2: +3V3 -> /Inputs/Signal_VCC
- D23 pad 3: /MotorDrv1/MOSI -> Net-(D23-Pad3)
- D24 pad 2: +3V3 -> /Inputs/Signal_VCC
- D24 pad 3: /MotorDrv1/CLK -> Net-(D24-Pad3)
- D26 pad 2: +3V3 -> /Inputs/Signal_VCC
- D26 pad 3: /Inputs/DIR_REFR -> Net-(D26-Pad3)
- D29 pad 2: +3V3 -> /Inputs/Signal_VCC
- D29 pad 3: /MotorDrv1/REFL_STEP -> Net-(D29-Pad3)
- J3 pad 2: /Inputs/DRV_ENN_raw -> Net-(J3-Pad2)
- J3 pad 4: (no net) -> Net-(J3-Pad4)
- J3 pad SH: GND -> Net-(C46-Pad1)
- J5 pad SH: GND -> Net-(C47-Pad1)
- R31 pad 1: Net-(R31-Pad1) -> /MotorDrv1/CLK
- R32 pad 1: Net-(R32-Pad1) -> /MotorDrv1/MOSI
- R33 pad 1: /MotorDrv1/DRV_ENA -> Net-(D20-Pad3)
- R33 pad 2: /Inputs/DRV_ENN_raw -> Net-(J3-Pad4)
- R34 pad 1: /MotorDrv1/MISO -> Net-(D21-Pad3)
- R35 pad 1: /Inputs/CSN -> Net-(D22-Pad3)
- R36 pad 1: /MotorDrv1/MOSI -> Net-(D23-Pad3)
- R37 pad 1: /MotorDrv1/CLK -> Net-(D24-Pad3)
- R39 pad 1: /Inputs/DIR_REFR -> Net-(D26-Pad3)
- R41 pad 1: Net-(R41-Pad1) -> /Inputs/CSN
- R42 pad 1: Net-(R42-Pad1) -> /MotorDrv1/MISO
- R43 pad 1: Net-(R43-Pad1) -> Net-(D15-Pad1)
- R43 pad 2: Net-(D15-Pad2) -> GND
- R44 pad 1: Net-(R44-Pad1) -> Net-(D16-Pad1)
- R44 pad 2: Net-(D16-Pad2) -> GND
- R45 pad 1: Net-(R45-Pad1) -> Net-(D17-Pad1)
- R45 pad 2: Net-(D17-Pad2) -> GND
- R46 pad 1: Net-(R46-Pad1) -> Net-(D18-Pad1)
- R46 pad 2: Net-(D18-Pad2) -> GND
- R47 pad 1: Net-(R47-Pad1) -> Net-(D19-Pad1)
- R47 pad 2: Net-(D19-Pad2) -> GND
- R49 pad 1: /MotorDrv1/REFL_STEP -> Net-(D29-Pad3)
- U5 pad 11: Net-(R47-Pad1) -> Net-(D19-Pad2)
- U6 pad 11: Net-(R42-Pad1) -> Net-(D21-Pad3)
- U6 pad 2: /MotorDrv1/CLK -> Net-(D24-Pad3)
- U6 pad 3: Net-(R31-Pad1) -> /MotorDrv1/CLK
- U6 pad 5: /MotorDrv1/MOSI -> Net-(D23-Pad3)
- U6 pad 6: Net-(R32-Pad1) -> /MotorDrv1/MOSI
- U6 pad 8: Net-(R41-Pad1) -> /Inputs/CSN
- U6 pad 9: /Inputs/CSN -> Net-(D22-Pad3)
- U7 pad 11: Net-(R46-Pad1) -> Net-(D18-Pad2)
- U7 pad 2: /MotorDrv1/DRV_ENA -> Net-(D20-Pad3)
- U7 pad 3: Net-(R43-Pad1) -> /MotorDrv1/DRV_ENA
- U7 pad 5: /Inputs/DIR_REFR -> Net-(D26-Pad3)
- U7 pad 6: Net-(R44-Pad1) -> /Inputs/DIR_REFR
- U7 pad 8: Net-(R45-Pad1) -> /MotorDrv1/REFL_STEP
- U7 pad 9: /MotorDrv1/REFL_STEP -> Net-(D29-Pad3)
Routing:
- net /Inputs/Signal_VCC: track 0.00 -> 87.6 mm, vias 0 -> 7
- net GND: track 292.5 -> 333.3 mm, vias 125 -> 111
- net Net-(R47-Pad1): track 32.7 -> 0.00 mm, vias 1 -> 0
- net Net-(D29-Pad3): track 0.00 -> 31.4 mm
- net Net-(R45-Pad1): track 27.0 -> 0.00 mm, vias 1 -> 0
- net Net-(D19-Pad2): track 2.23 -> 28.5 mm, vias 0 -> 2
- net Net-(D21-Pad3): track 0.00 -> 26.1 mm, vias 0 -> 2
- net Net-(R32-Pad1): track 23.7 -> 0.00 mm, vias 1 -> 0
- net Net-(D22-Pad3): track 0.00 -> 23.4 mm, vias 0 -> 2
- net Net-(C46-Pad1): track 0.00 -> 22.7 mm
- net Net-(C47-Pad1): track 0.00 -> 22.5 mm
- net Net-(R31-Pad1): track 21.4 -> 0.00 mm, vias 1 -> 0
- net Net-(R43-Pad1): track 20.3 -> 0.00 mm, vias 1 -> 0
- net Net-(D26-Pad3): track 0.00 -> 19.8 mm, vias 0 -> 2
- net Net-(R42-Pad1): track 19.6 -> 0.00 mm, vias 1 -> 0
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- added copper zone on B.Cu, net Net-(F1-Pad2)
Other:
- board text added: "+"
- board text added: "-"
- board text added: "TMC5160 Stepper Driver 48V 6A MAX"
- board text added: "github.com/pommen"

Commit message: Ver0.1 done
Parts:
- C37: footprint peters:D_0805_peter -> peters:C_0805_peter
- TP1, TP2: footprint TestPoint:TestPoint_Pad_1.5x1.5mm -> TestPoint:TestPoint_Pad_D1.5mm
- TP7: footprint TestPoint:TestPoint_Pad_1.5x1.5mm -> TestPoint:TestPoint_THTPad_1.5x1.5mm_Drill0.7mm
- moved C2 0.63 mm to (89.8, 71.9)
- moved R19 0.13 mm to (98.3, 88.8)
- moved JP2 0.13 mm to (111.4, 129.9)
- moved C37 0.11 mm to (98.3, 90.9)
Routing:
- net GND: track 333.3 -> 353.8 mm, vias 111 -> 119
- net +3V3: track 40.6 -> 44.0 mm, vias 14 -> 15
- net +5V: track 109.6 -> 107.5 mm
- net Net-(JP2-Pad2): track 39.2 -> 41.2 mm
- net Net-(C40-Pad1): track 45.6 -> 43.6 mm
- net Net-(C40-Pad2): track 42.1 -> 40.7 mm
- net Net-(C37-Pad1): track 8.49 -> 9.23 mm
- net +48V: track 60.3 -> 59.8 mm
- added copper zone on In2.Cu, net GND
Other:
- board text added: "0"
- board text added: "1"
- board text added: "See TMC5160 datasheet for SD_MODE and SPI_MODE CFG page 13"
